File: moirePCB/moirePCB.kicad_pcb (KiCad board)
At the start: 4 copper layers, 32 x 228.8 mm, 55 parts, among them J1 USB_C_Receptacle, U1 ESP32-PICO-D4, U10 TLV73333PDBV, U2 BQ25504, U3 TLV73333PDBV, U4 RFM95W-915S2, U5 CH340E, U6 TLC555xD, U7 HDC1080, U8 AP2281-1WG-7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

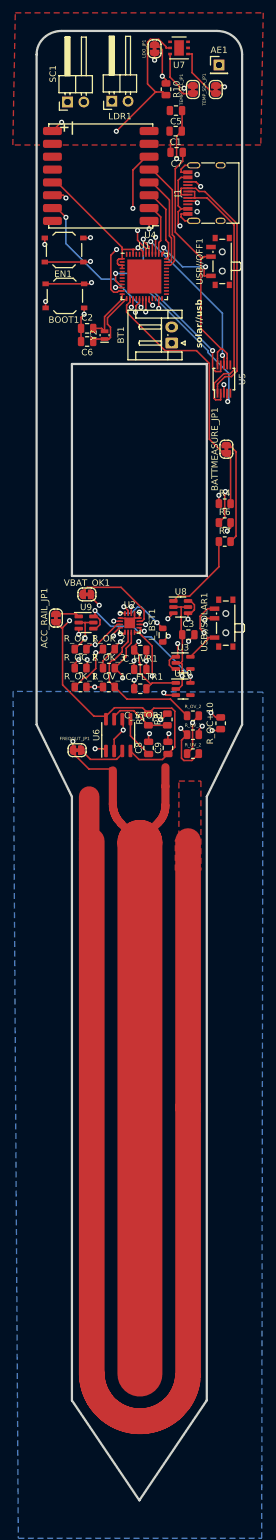
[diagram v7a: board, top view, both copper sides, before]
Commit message: rounded bat hole and screw holes
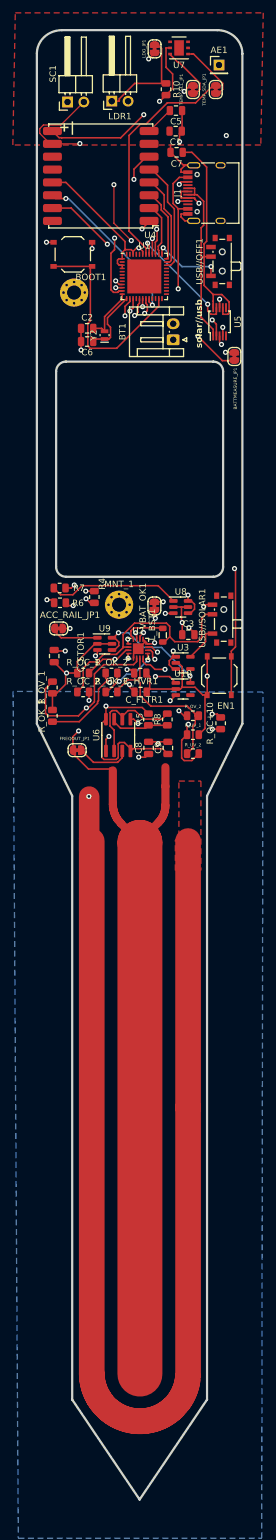
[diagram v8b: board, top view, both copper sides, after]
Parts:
- added MNT_1: MountingHole_2.2mm_M2_Pad_Via, MountingHole:MountingHole_2.2mm_M2_Pad_Via, F.Cu at (52.0, 101.3)
- added MNT_2: MountingHole_2.2mm_M2_Pad_Via, MountingHole:MountingHole_2.2mm_M2_Pad_Via, F.Cu at (45.0, 52.7)
- moved EN1 70.5 mm to (67.6, 112.3), turned to 90 degrees
- moved R6 28.5 mm to (42.8, 101.0)
- moved R7 26.7 mm to (42.8, 98.7)
- moved R4 25.0 mm to (48.1, 100.1), turned to -90 degrees
- moved BATTMEASURE_JP1 14.5 mm to (70.0, 62.6)
- moved C_STOR1 14.3 mm to (41.9, 109.3), turned to 90 degrees
- moved VBAT_OK1 10.7 mm to (57.5, 101.5), turned to 90 degrees
- moved U5 8.94 mm to (67.7, 57.2)
- moved R_OV_1 8.79 mm to (41.6, 114.2), turned to 90 degrees
- moved BOOT1 6.58 mm to (44.8, 46.8), turned to 180 degrees
- moved R_OK_1 6.27 mm to (41.6, 118.6), turned to 90 degrees
- moved U9 4.41 mm to (49.8, 107.4)
- moved U2 4.24 mm to (55.0, 108.2)
- moved R_OC_1 3.74 mm to (46.4, 111.9)
- moved R_OK_2 3.74 mm to (50.8, 111.9)
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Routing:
- net GND: track 313.3 -> 370.7 mm
- net Net-(BATTMEASURE_JP1-B): track 16.3 -> 61.5 mm, vias 0 -> 2
- net /EN: track 44.3 -> 81.6 mm
- net BATT_MEASURE: track 42.0 -> 77.6 mm, vias 0 -> 3
- net Net-(J1-CC2): track 56.6 -> 76.4 mm
- net Net-(J1-CC1): track 56.5 -> 75.9 mm
- net Net-(U2-VBAT_OV): track 23.4 -> 42.5 mm, vias 0 -> 2
- net /D-: track 42.0 -> 27.1 mm, vias 0 -> 2
- net /D+: track 41.3 -> 26.8 mm
- net Net-(U1-IO0): track 21.1 -> 33.7 mm, vias 2 -> 0
- net /TX: track 29.8 -> 18.9 mm
- net Net-(U10-IN): track 20.7 -> 29.7 mm, vias 2 -> 4
- net Net-(SC1-+): track 133.6 -> 124.7 mm
- net VCC: track 153.8 -> 162.2 mm
- net /RX: track 26.0 -> 18.3 mm
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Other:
- outline, holes or cut-outs redrawn
